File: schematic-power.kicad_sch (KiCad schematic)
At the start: 32 parts, among them U4 TPS62933, U9 TPS62933

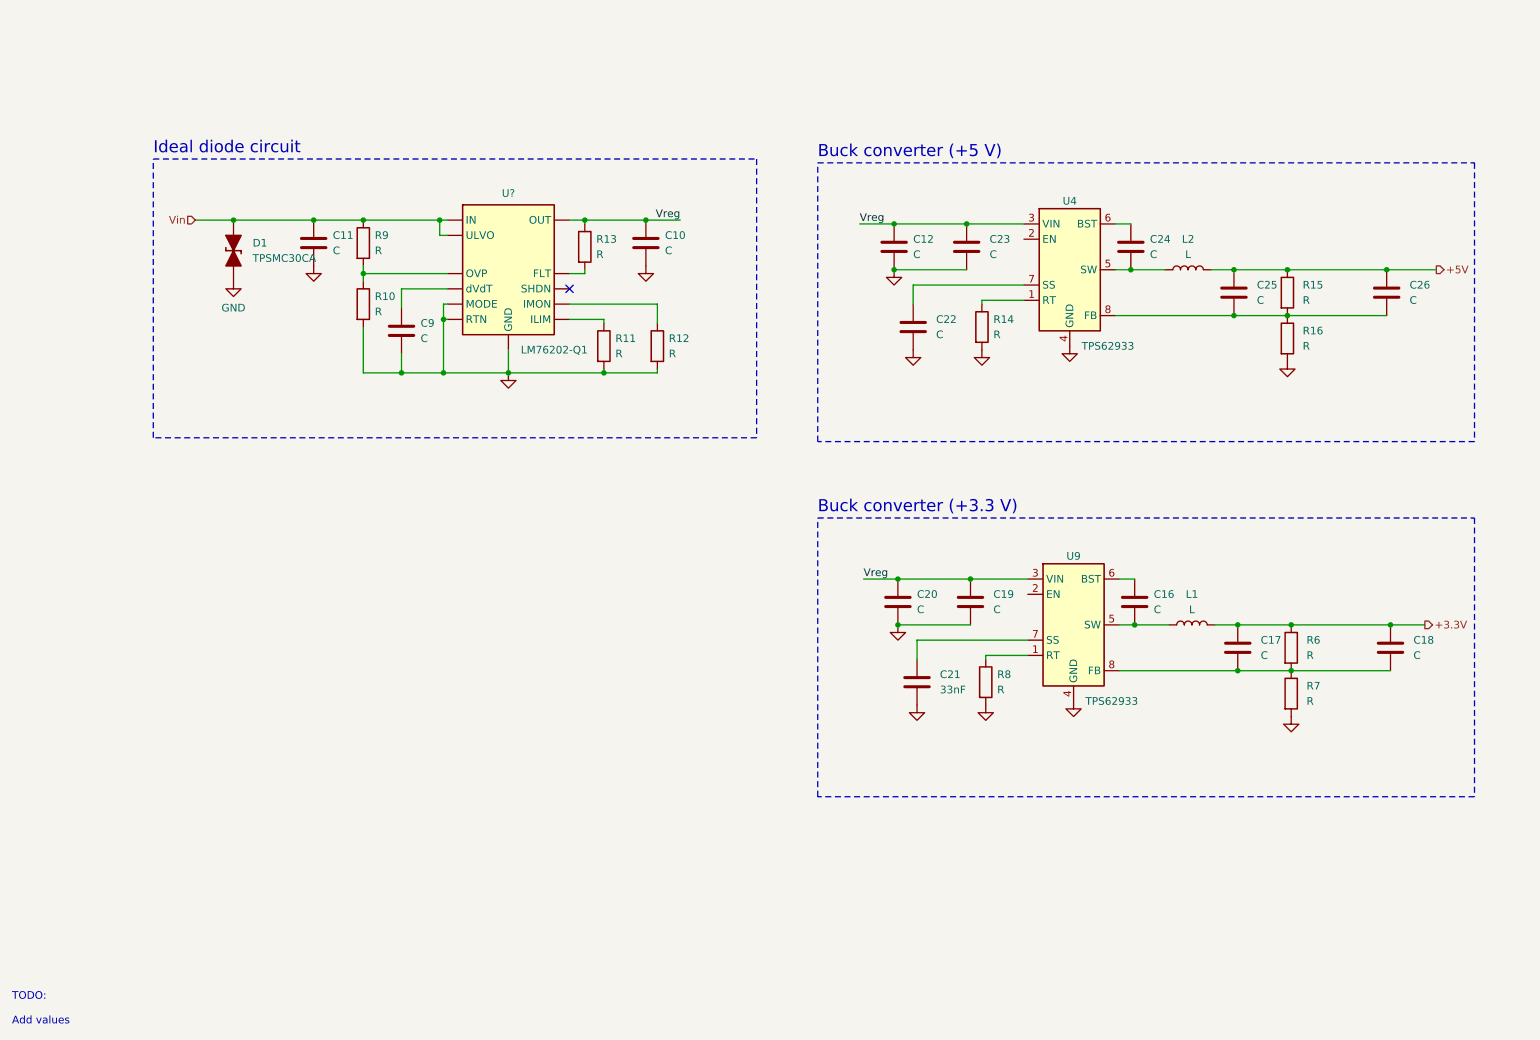
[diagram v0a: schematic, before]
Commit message: First converter version
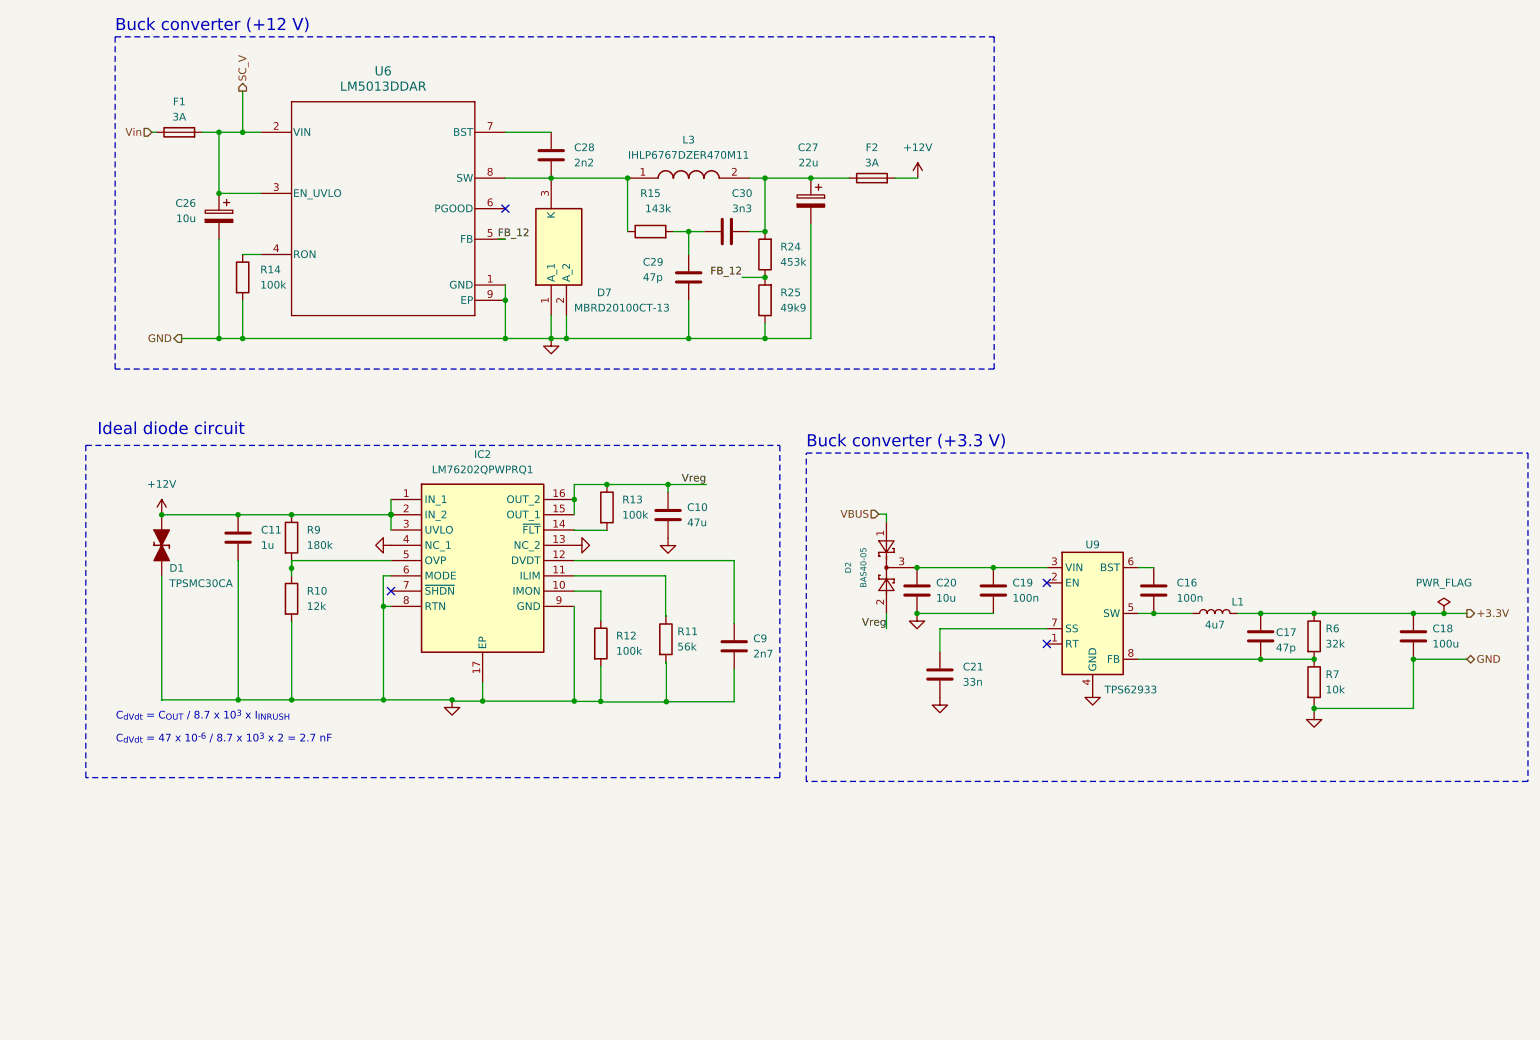
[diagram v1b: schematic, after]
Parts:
- removed C12, C22, C23, C24, C25, C26: C, symbol Device:C
- removed L2: L, symbol Device:L
- removed R16, R8: R, symbol Device:R
- removed U4: TPS62933, Package_TO_SOT_SMD:SOT-583-8, symbol Regulator_Switching:TPS62933
- removed U?: LM76202-Q1, symbol Hydros:LM76202-Q1
- added C26: 10u, Capacitor_SMD:CP_Elec_8x10.5, symbol Device:C_Polarized
- added C27: 22u, Capacitor_SMD:CP_Elec_8x10.5, symbol Device:C_Polarized
- added C28: 2n2, Capacitor_SMD:C_1206_3216Metric, symbol Device:C
- added C29: 47p, Capacitor_SMD:C_1206_3216Metric, symbol Device:C
- added C30: 3n3, Capacitor_SMD:C_1206_3216Metric, symbol Device:C
- added D2: BAS40-05, Package_TO_SOT_SMD:SOT-23, symbol Diode:BAS40-04
- added D7: MBRD20100CT-13, MBRD20100CT-13:TO252_(DPAK)_1, symbol MBRD20100CT-13:MBRD20100CT-13
- added F1, F2: 3A, mbr:FUSC8664X180N, symbol Device:Fuse
- added IC2: LM76202QPWPRQ1, mbr:SOP65P640X120-17N, symbol Lm7602 ideal diode:LM76202QPWPRQ1
- added L3: IHLP6767DZER470M11, library:IHLP6767DZER470M11, symbol IHLP6767DZER470M11:IHLP6767DZER470M11
- added R24: 453k, LED_SMD:LED_1206_3216Metric, symbol Device:R
- added R25: 49k9, LED_SMD:LED_1206_3216Metric, symbol Device:R
- added U6: LM5013DDAR, Package_SO:Diodes_SO-8EP, symbol 2023-11-20_17-31-45:LM5013DDAR
- C10: value C -> 47u; footprint (none) -> Capacitor_SMD:CP_Elec_6.3x7.7
- C11: value C -> 1u; footprint (none) -> Capacitor_SMD:C_1206_3216Metric
- C16, C19: value C -> 100n; footprint (none) -> Capacitor_SMD:C_1206_3216Metric
- C17: value C -> 47p; footprint (none) -> Capacitor_SMD:C_1206_3216Metric
- C18: value C -> 100u; footprint (none) -> Capacitor_SMD:CP_Elec_8x10.5
- C20: value C -> 10u; footprint (none) -> Capacitor_SMD:CP_Elec_8x10.5
- C21: value 33nF -> 33n; footprint (none) -> Capacitor_SMD:C_1206_3216Metric
- C9: value C -> 2n7; footprint (none) -> Capacitor_SMD:C_1206_3216Metric
- D1: footprint Diode_SMD_AKL:D_SMC_TVS -> lib:TPSMCSeries_LTF
- L1: value L -> 4u7; footprint (none) -> library:SRN3015TA4R7M
- R10: value R -> 12k; footprint (none) -> Resistor_SMD:R_1206_3216Metric
- R11: value R -> 56k; footprint (none) -> Resistor_SMD:R_1206_3216Metric
- R12, R13, R14: value R -> 100k; footprint (none) -> Resistor_SMD:R_1206_3216Metric
- R15: value R -> 143k; footprint (none) -> Resistor_SMD:R_1206_3216Metric
- R6: value R -> 32k; footprint (none) -> Resistor_SMD:R_1206_3216Metric
- R7: value R -> 10k; footprint (none) -> Resistor_SMD:R_1206_3216Metric
- R9: value R -> 180k; footprint (none) -> Resistor_SMD:R_1206_3216Metric
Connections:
- net GND: now also C18.2, C26.2, C27.2, C29.1, D7.1 (A_1), D7.2 (A_2), IC2.13 (NC_2), IC2.17 (EP), IC2.4 (NC_1), IC2.6 (MODE), IC2.8 (RTN), IC2.9 (GND), R25.1, U6.1 (GND), U6.9 (EP)
- net Vin: now also F1.1; no longer C11.1, D1.2 (A), R9.1
- net Vreg: now also D2.2, IC2.15 (OUT_1), IC2.16 (OUT_2); no longer C19.1, C20.1, U9.3 (VIN)
- net at C9.1: now also IC2.12 (DVDT)
- net at R13.2: now also IC2.14 (~{FLT})
- net at R12.1: now also IC2.10 (IMON)
- net at R10.1, R9.2: now also IC2.5 (OVP)
- net at R11.1: now also IC2.11 (ILIM)
- net at R14.1: now also U6.4 (RON)
- net at R15.2: now also C29.2, C30.1
- net at C17.2, R6.2, R7.1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: no longer C18.2
- net +5V: no longer names the net of R15.1
- net +5V: now also C28.1, D7.3 (K), L3.1, U6.8 (SW)
- new net: C27.1, C30.2, F2.1, L3.2, R24.2
- new net: C19.1, C20.1, D2.3, U9.3 (VIN)
- new net: C28.2, U6.7 (BST)
- new net +12V: C11.1, D1.2 (A), F2.2, IC2.1 (IN_1), IC2.2 (IN_2), IC2.3 (UVLO), R9.1
- new net FB_12: R24.1, R25.2, U6.5 (FB)
- new net SC_V: C26.1, F1.2, U6.2 (VIN), U6.3 (EN_UVLO)
- new net VBUS: D2.1
- no-connect marks 1 -> 4
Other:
- note added: "Buck converter (+12 V)"
- note added: "C_{dVdt} = 47 x 10^{-6} / 8.7 x 10^{3} x 2 = 2.7 nF"
- note added: "C_{dVdt} = C_{OUT} / 8.7 x 10^{3} x I_{INRUSH}"
- note removed: "Buck converter (+5 V)"
- note removed: "TODO: Add values"
- company: (none) -> Hydrogreen Pollub
- title: (none) -> Fuel Cell Control Unit  (FCCU)
- moved on the sheet: C10, C11, C16, C17, C18, C19, C20, C21, C9, D1, L1, R10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
